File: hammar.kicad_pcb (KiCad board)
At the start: 2 copper layers, 97.5 x 53.8 mm, 115 parts, among them J1 Conn_01x08_Female, J10 YMIN, J11 ZMIN, J12 X, J13 Y, J14 Z, J15 E, J2 Conn_02x12_Odd_Even, J3 Z, J5 TEND, J7 TBED, J8 USB_C_Receptacle_USB2.0, J9 XMIN, Q1 Q_NMOS_GDS, Q2 Q_NMOS_GSD, Q3 Q_NMOS_GDS, SW1 SW_MEC_5G, SW2 SW_MEC_5G, U1 A4988, U2 ESP32-S2, U3 A4988, U4 A4988, U5 A4988, U6 3,3v lin, Y1 Crystal_GND24_Small

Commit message: Redesign
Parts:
- removed AE1: Antenna_Shield, MyAntennas:SWRU120B
- removed C11, C14, C5, C8, C9: 100nF, Capacitor_SMD:C_0603_1608Metric
- removed C16, C17: 1µF, Capacitor_SMD:C_0603_1608Metric
- removed C2: 15pF, Capacitor_SMD:C_0603_1608Metric
- removed C3: 1pF, Capacitor_SMD:C_0603_1608Metric
- removed SW2: SW_MEC_5G, Button_Switch_THT:SW_PUSH_6mm
- added G***: LOGO, LOGO, B.Cu at (110.8, 101.5)
- added J16: UART, Connector_PinHeader_2.54mm:PinHeader_1x04_P2.54mm_Vertical, B.Cu at (151.2, 99.7)
- added J6: Conn_01x03_Male, Connector_PinHeader_2.54mm:PinHeader_1x03_P2.54mm_Vertical, B.Cu at (97.3, 106.8)
- added Q4: Q_NPN_BEC, Package_TO_SOT_SMD:SOT-23, F.Cu at (137.7, 92.2)
- added Q5: Q_NPN_BEC, Package_TO_SOT_SMD:SOT-23, F.Cu at (133.7, 92.2)
- added R10: 22Ω, Resistor_SMD:R_0603_1608Metric, F.Cu at (172.0, 113.7)
- added R22: 1kΩ, Resistor_SMD:R_0603_1608Metric, F.Cu at (158.2, 113.0)
- added R34: 1kΩ, Resistor_SMD:R_0603_1608Metric, F.Cu at (123.0, 96.7)
- added R39: 680Ω, Resistor_SMD:R_0603_1608Metric, F.Cu at (106.8, 101.0)
- added R4: 22Ω, Resistor_SMD:R_0603_1608Metric, F.Cu at (172.0, 112.2)
- added R40: 10kΩ, Resistor_SMD:R_0603_1608Metric, F.Cu at (140.7, 92.2)
- added R41: 10kΩ, Resistor_SMD:R_0603_1608Metric, F.Cu at (130.7, 92.2)
- added R42: 10kΩ, Resistor_SMD:R_0603_1608Metric, F.Cu at (119.5, 102.2)
- added R43: 10kΩ, Resistor_SMD:R_0603_1608Metric, F.Cu at (121.5, 99.7)
- added U7: CH340G, Package_SO:SOIC-16_3.9x9.9mm_P1.27mm, F.Cu at (165.2, 113.0)
- added Z: ZMIN_probe, Connector_PinHeader_2.54mm:PinHeader_1x03_P2.54mm_Vertical, B.Cu at (101.7, 112.5)
- C1: value 15pF -> 100nF
- C15, C29, C30: footprint Capacitor_SMD:C_0603_1608Metric -> Capacitor_SMD:C_0805_2012Metric
- D5: value LED_Small -> D_Zener_~3,3v; footprint DIY:LED 0603 reverse mount -> Diode_SMD:D_SOD-323
- J11: value ZMIN -> I2C/SPI; footprint Connector_JST:JST_PH_S3B-PH-K_1x03_P2.00mm_Horizontal -> Connector_PinHeader_2.54mm:PinHeader_1x08_P2.54mm_Vertical; moved to B.Cu
- J12, J14, J15: footprint Connector_JST:JST_PH_S4B-PH-K_1x04_P2.00mm_Horizontal -> Connector_PinHeader_2.54mm:PinHeader_1x04_P2.54mm_Vertical; moved to B.Cu
- J2: value Conn_02x12_Odd_Even -> Micro_SD_Card; footprint Connector_PinHeader_2.54mm:PinHeader_2x12_P2.54mm_Vertical -> DIY:microSD
- J3: footprint Connector_JST:JST_PH_B4B-PH-K_1x04_P2.00mm_Vertical -> Connector_PinHeader_2.54mm:PinHeader_1x04_P2.54mm_Vertical; moved to B.Cu
- J5, J7: footprint Connector_JST:JST_PH_S2B-PH-K_1x02_P2.00mm_Horizontal -> Connector_PinHeader_2.54mm:PinHeader_1x02_P2.54mm_Vertical; moved to B.Cu
- Jw: renamed from J13; footprint Connector_JST:JST_PH_S4B-PH-K_1x04_P2.00mm_Horizontal -> Connector_PinHeader_2.54mm:PinHeader_1x04_P2.54mm_Vertical; moved to B.Cu
- R11: value 10kΩ -> 1kΩ
- R26: value 1kΩ -> 10kΩ
- SW1: moved to B.Cu
- U2: value ESP32-S2 -> ESP32-WROOM-32; footprint Package_DFN_QFN:QFN-56-1EP_7x7mm_P0.4mm_EP5.6x5.6mm -> RF_Module:ESP32-WROOM-32
- U6: footprint Package_TO_SOT_SMD:TO-252-2 -> DIY:mini BUCK
- X: renamed from J9; footprint Connector_JST:JST_PH_S3B-PH-K_1x03_P2.00mm_Horizontal -> Connector_PinHeader_2.54mm:PinHeader_1x03_P2.54mm_Vertical; moved to B.Cu
- Y: renamed from J10; footprint Connector_JST:JST_PH_S3B-PH-K_1x03_P2.00mm_Horizontal -> Connector_PinHeader_2.54mm:PinHeader_1x03_P2.54mm_Vertical; moved to B.Cu
- Y1: value Crystal_GND24_Small -> Resonator_Small; footprint Crystal:Crystal_SMD_3225-4Pin_3.2x2.5mm -> DIY:resonator_3,2x1,3
- moved R11 54.5 mm to (158.2, 111.2), turned to 0 degrees
- moved Y1 51.9 mm to (172.0, 116.5), turned to 90 degrees
- moved J11 45.2 mm to (127.2, 112.2), turned to 0 degrees
- moved C1 45.1 mm to (165.5, 117.7)
- moved R26 41.2 mm to (145.7, 91.7), turned to 0 degrees
- moved C15 41.1 mm to (151.5, 110.5), turned to 0 degrees
- moved C12 37.8 mm to (151.2, 112.2)
- moved U2 29.6 mm to (139.2, 104.7), turned to 180 degrees
- moved C32 26.8 mm to (159.2, 100.5), turned to 180 degrees
- moved R25 25.8 mm to (170.0, 106.2), turned to 90 degrees
- moved SW1 23.6 mm to (117.3, 100.0), turned to 90 degrees
- moved R15 23.1 mm to (124.5, 96.7)
- moved C37 22.9 mm to (158.2, 98.7), turned to 0 degrees
- moved C22 21.7 mm to (121.5, 96.7)
- moved Q2 21.6 mm to (171.2, 93.5)
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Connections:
- C1 pad 2: Net-(C1-Pad2) -> +3.3V
- C22 pad 2: RST -> Net-(C22-Pad2)
- D5 pad 1: Net-(D5-Pad1) -> Z-MIN
- D5 pad 2: IO13 -> GND
- F2 pad 2: BEDCONN-F -> VIN
- J1 pad 3: +VDC -> BEDCONN
- J1 pad 4: BEDCONN -> BEDCONN-F
- J11 pad 3: Z-MIN -> SCL
- J2 pad 1: IO33 -> unconnected-(J2-Pad1)
- J2 pad 2: IO46 -> SS
- J2 pad 3: IO32/SPID -> MOSI
- J2 pad 4: IO45 -> +3.3V
- J2 pad 5: IO31/SPIQ -> SCK
- J2 pad 6: IO44/U0RXD -> GND
- J2 pad 7: IO30/SPICLK -> MISO
- J2 pad 8: IO43/U0TXD -> unconnected-(J2-Pad8)
- J2 pad 9: IO29/SPICLK -> unconnected-(J2-Pad9)
- R11 pad 1: Net-(R11-Pad1) -> TX
- R11 pad 2: +3.3V -> Net-(R11-Pad2)
- R15 pad 2: RST -> Net-(C22-Pad2)
- R26 pad 2: Net-(D5-Pad1) -> Z-DIR
- SW1 pad 1: RST -> Net-(C22-Pad2)
- U2 pad 1: +3.3V -> GND
- U2 pad 10: Y-DIR -> E-EN
- U2 pad 11: Z-STP -> X-DIR
- U2 pad 12: Z-DIR -> X-STP
- U2 pad 13: E-STP -> Z-STP
- U2 pad 14: E-DIR -> Z-DIR
- U2 pad 15: E-EN -> GND
- U2 pad 16: T-BED -> FAN
- U2 pad 17: END -> unconnected-(U2-Pad17)
- U2 pad 18: IO13 -> unconnected-(U2-Pad18)
- U2 pad 19: FAN -> unconnected-(U2-Pad19)
- U2 pad 2: Net-(AE1-Pad1) -> +3.3V
- U2 pad 20: +3.3V -> unconnected-(U2-Pad20)
- U2 pad 21: Z-MIN -> unconnected-(U2-Pad21)
- U2 pad 22: BED -> unconnected-(U2-Pad22)
- U2 pad 23: unconnected-(U2-Pad23) -> Z-MIN
- U2 pad 24: Net-(R11-Pad1) -> END
- U2 pad 25: D- -> IO0
- U2 pad 26: D+ -> BED
- U2 pad 27: +3.3V -> E-STP
- U2 pad 28: IO21 -> E-DIR
- U2 pad 29: IO26/SPI_CS1 -> SS
- U2 pad 3: +3.3V -> RST
- U2 pad 30: unconnected-(U2-Pad30) -> SCK
- U2 pad 31: IO27/SPIHD -> MISO
- U2 pad 32: IO28/SPIWP -> unconnected-(U2-Pad32)
- U2 pad 33: IO29/SPICLK -> SDA
- U2 pad 34: IO30/SPICLK -> TX
- U2 pad 35: IO31/SPIQ -> RX
- U2 pad 36: IO32/SPID -> SCL
- U2 pad 37: IO33 -> MOSI
- U2 pad 38: X-MIN -> GND
- U2 pad 39: Y-MIN -> GND
- U2 pad 4: +3.3V -> T-END
- U2 pad 5: BOOT -> T-BED
- U2 pad 6: T-END -> X-MIN
- U2 pad 7: X-STP -> Y-MIN
- U2 pad 8: X-DIR -> Y-DIR
- Y1 pad 1: Net-(C2-Pad2) -> Net-(U7-Pad7)
- Y1 pad 3: Net-(C1-Pad2) -> Net-(U7-Pad8)
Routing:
- net +VDC: track 205.2 -> 274.1 mm, vias 19 -> 23
- net D+: track 82.5 -> 14.4 mm, vias 2 -> 0
- net D-: track 78.2 -> 13.8 mm, vias 2 -> 0
- net DTR: track 0.00 -> 54.9 mm, vias 0 -> 2
- net RTS: track 0.00 -> 47.6 mm, vias 0 -> 2
- net TX: track 0.00 -> 41.6 mm, vias 0 -> 3
- net RX: track 0.00 -> 41.1 mm, vias 0 -> 3
- net MISO: track 0.00 -> 39.1 mm, vias 0 -> 1
- net Net-(AE1-Pad1): track 38.0 -> 0.00 mm
- net BOOT: track 36.7 -> 0.00 mm, vias 1 -> 0
- net IO40/JTAG/MTDO: track 34.7 -> 0.00 mm, vias 1 -> 0
- net IO39/JTAG/MTCK: track 34.3 -> 0.00 mm, vias 1 -> 0
- net IO41/JTAG/MTDI: track 30.3 -> 0.00 mm, vias 1 -> 0
- net IO42/JTAG/MTMS: track 29.2 -> 0.00 mm, vias 1 -> 0
- net MOSI: track 0.00 -> 29.2 mm, vias 0 -> 2
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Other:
- board size 97.5 x 53.8 mm -> 97.5 x 55 mm
- board text added: "+ -"
- board text added: "- +"
- board text added: "0"
- board text added: "End"
- board text added: "Hammar v1,1"
- board text added: "MISO"
- board text added: "MOSI"
- board text added: "RX"
- board text added: "S"
- board text added: "SCK"
- board text added: "SCL"
- board text added: "SDA"
- board text added: "TX"
- board text added: "VCC"
- board text added: "VIN"
- board text added: "Z voltage 3,3V VIN"
- board text removed: "- VIN +"
- board text removed: "17"
- board text removed: "21"
- board text removed: "26"
- board text removed: "27"
- board text removed: "28"
- board text removed: "29"
- board text removed: "30"
- board text removed: "31"
- board text removed: "32"
- board text removed: "33"
- board text removed: "36"
- board text removed: "37"
- board text removed: "38"
- board text removed: "39"
- board text removed: "40"
- board text removed: "41"
- board text removed: "42"
- board text removed: "43"
- board text removed: "44"
- board text removed: "45"
- board text removed: "46"
- board text removed: "BED"
- board text removed: "END"
- board text removed: "Hammar v1"
- board text removed: "S GND 3,3V"
- board text removed: "Test"

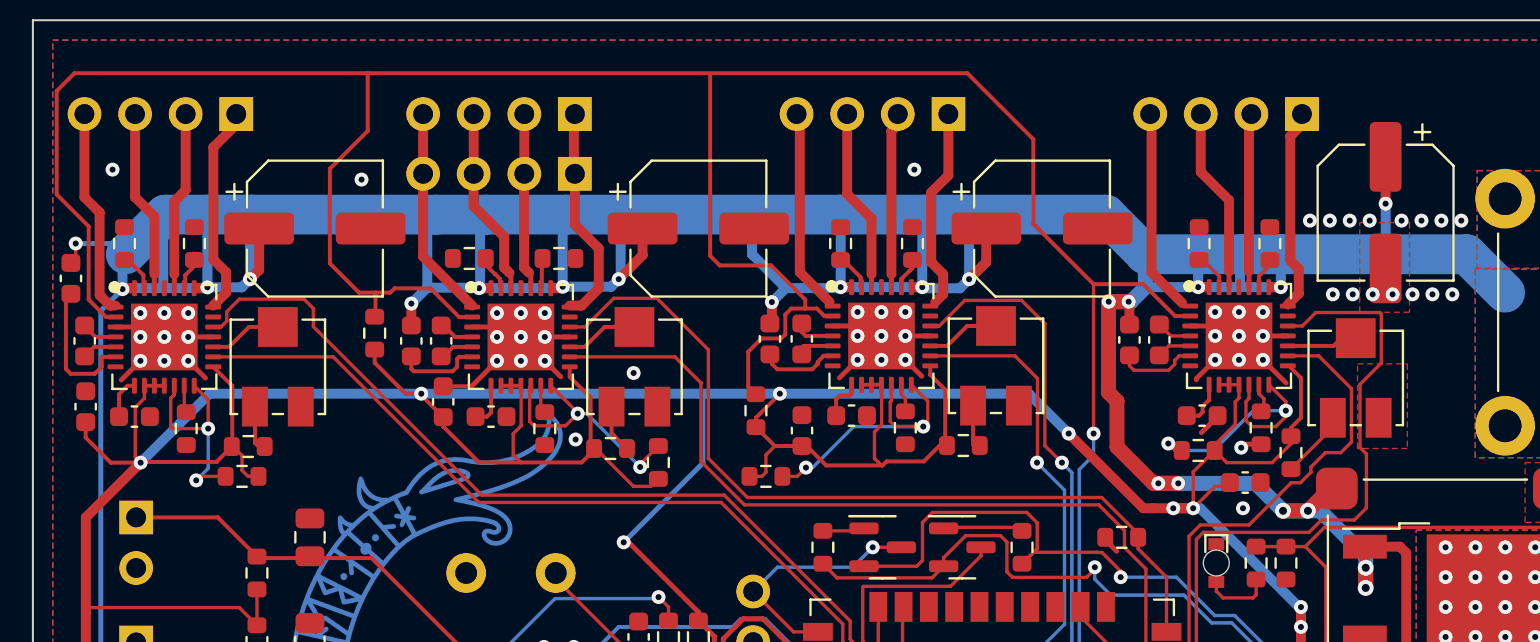
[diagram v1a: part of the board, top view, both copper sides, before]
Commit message: changed designators and updated BOM
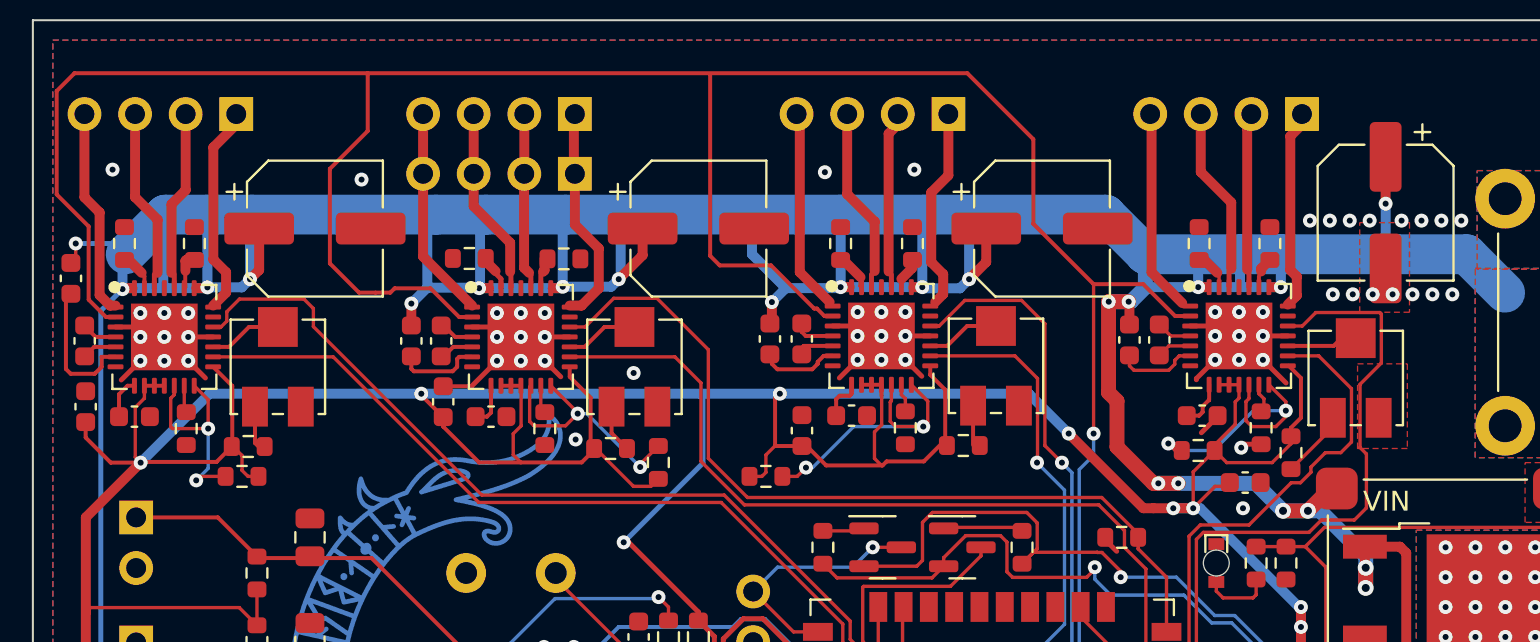
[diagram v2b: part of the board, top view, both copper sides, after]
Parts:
- removed the R34 at (108.2, 81.5)
- removed the R4 at (127.4, 85.4)
- D3: renamed from D5; value D_Zener_~3,3v -> Zener_~3,3v
- D6: value D_Small -> USB protection diode, >500mA 24V
- F1: value Fuse_Small -> 25A Mini fuse + Keystone 3557 fuse holders, or equivalent
- F2: value Fuse_Small -> 15A Mini fuse + Keystone 3557 fuse holders, or equivalent
- F3: value Polyfuse_Small -> Polyfuse 500mA
- J1: value Conn_01x08_Female -> 8x screw terminal, 5,08mm spacing. rated for >20A
- J2: value Micro_SD_Card -> Micro_SD_Holder
- Q1: renamed from Q5; value Q_NPN_BEC -> S9014 or equivalent
- Q2: renamed from Q4; value Q_NPN_BEC -> S9014 or equivalent
- Q3: renamed from Q2; value Q_NMOS_GSD -> TI CSD17310Q5A or equivalent
- Q4: renamed from Q1; value Q_NMOS_GDS -> PMV40UN2R or equivalent
- Q5: renamed from Q3; value Q_NMOS_GDS -> PMV40UN2R or equivalent
- RV1: renamed from RV2; value R_Potentiometer_Small -> Potentiometer_10kΩ
- RV2: renamed from RV4; value R_Potentiometer_Small -> Potentiometer_10kΩ
- RV3: value R_Potentiometer_Small -> Potentiometer_10kΩ
- RV4: renamed from RV1; value R_Potentiometer_Small -> Potentiometer_10kΩ
- RV5, RV6: value Varistor -> ESD varistor, optional
- U5: renamed from U6; value 3,3v lin -> DPAK 3,3v linear regulator + caps OR mini buck converter
- U6: renamed from U2; value ESP32-WROOM-32 -> ESP32-WROOM-32E
- Y1: value Resonator_Small -> Resonator_12mhz
- moved G*** 0.39 mm to (138.9, 100.6)
- moved R8 0.25 mm to (117.7, 77.7)
- renumbered C10 to C1, C31 to C10, C26 to C11, C24 to C12, C28 to C13, C36 to C14, C19 to C15, C6 to C16, C33 to C17, C25 to C18, C23 to C19, C35 to C2, C13 to C20, C29 to C21, C30 to C23, C37 to C24, C32 to C25, C15 to C26, C12 to C27, C1 to C28, C21 to C3, C27 to C4, C34 to C5, C20 to C6, C18 to C7, C7 to C8, C4 to C9, D2 to D1, D1 to D2, D3 to D4, D4 to D5, J7 to J10, J16 to J11, J6 to J12, J11 to J13, X to J14, Z to J15, Y to J16, J8 to J3, J12 to J4, Jw to J5, J14 to J6, J15 to J7, J3 to J8, J5 to J9, R37 to R1, R3 to R10, R33 to R11, R21 to R12, R8 to R13, R31 to R14, R18 to R15, R1 to R16, R2 to R17, R17 to R18, R30 to R19, R38 to R2, R7 to R20, R26 to R21, R41 to R22, R40 to R23, R19 to R24, R20 to R25, R29 to R26, R14 to R27, R13 to R28, R34 to R29, R12 to R3, R15 to R30, R32 to R31, R43 to R32, R39 to R33, R42 to R34, R24 to R35, R23 to R36, R25 to R37, R11 to R38, R4 to R39, R16 to R4, R35 to R40, R22 to R41, R10 to R42, R36 to R43, R27 to R7, R28 to R8, U3 to U1, U1 to U2, U5 to U3
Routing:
- net E-EN: track 146.4 -> 138.2 mm
- net +3.3V: track 380.3 -> 375.8 mm
- net GND: vias 96 -> 97
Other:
- board text added: "RST"

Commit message: little fix
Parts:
- J10: value TBED -> 1x2
- J11: value UART -> 1x4
- J12: value Conn_01x03_Male -> 1x3
- J13: value I2C/SPI -> 1x8
- J14: value XMIN -> 1x3
- J15: value ZMIN_probe -> 1x3
- J16: value YMIN -> 1x3
- J4: value X -> 1x4
- J5: value Y -> 1x4
- J6, J8: value Z -> 1x4
- J7: value E -> 1x4
- J9: value TEND -> 1x2
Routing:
- net E-EN: track 138.2 -> 137.4 mm

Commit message: updated bom++
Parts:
- D6: value USB protection diode, >500mA 24V -> USB protection diode, >500mA >24V. Silicon fine
- F1: value 25A Mini fuse + Keystone 3557 fuse holders, or equivalent -> 15A Mini fuse + Keystone 3557 fuse holders, or equivalent
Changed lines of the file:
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@@
       (effects (font (size 1 1) (thickness 0.15)))
     )
-    (fp_text value "USB protection diode, >500mA 24V" (at -0.25 2.25) (layer "F.Fab")
+    (fp_text value "USB protection diode, >500mA >24V. Silicon fine" (at -0.25 2.25) (layer "F.Fab")
       (effects (font (size 1 1) (thickness 0.15)))
     )
@@
       (effects (font (size 1 1) (thickness 0.15)))
     )
-    (fp_text value "25A Mini fuse + Keystone 3557 fuse holders, or equivalent" (at 0 -4 -90 unlocked) (layer "F.Fab")
-      (effects (font (size 1 1) (thickness 0.15)))
-    )
+    (fp_text value "15A Mini fuse + Keystone 3557 fuse holders, or equivalent" (at 0 -4 -90 unlocked) (layer "F.Fab")
+      (effects (font (size 1 1) (thickness 0.15)))
+    )

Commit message: slight reference update
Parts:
- moved J3 0.25 mm to (185.6, 115.0)
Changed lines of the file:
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@@
   )
   (footprint "Connector_USB:USB_C_Receptacle_HRO_TYPE-C-31-M-12" (layer "F.Cu")
-    (at 185.865 114.972756 90)
+    (at 185.615 114.972756 90)
     (descr "USB Type-C receptacle for USB 2.0 and PD, http://www.krhro.com/uploads/soft/180320/1-1P320120243.pdf")
     (tags "usb usb-c 2.0 pd")
@@
   (segment (start 117.305 93.80897) (end 117.305 93.512874) (width 0.17) (layer "F.Cu") (net 28))
   (segment (start 121.202709 97.460465) (end 118.6503 100.012874) (width 0.17) (layer "F.Cu") (net 28))
-  (segment (start 180.715 116.472756) (end 180.965 116.222756) (width 0.25) (layer "F.Cu") (net 29))
-  (segment (start 177.805 116.687874) (end 178.53 117.412874) (width 0.25) (layer "F.Cu") (net 29))
-  (segment (start 178.53 117.412874) (end 179.797462 117.412874) (width 0.25) (layer "F.Cu") (net 29))
-  (segment (start 180.965 116.222756) (end 181.82 116.222756) (width 0.25) (layer "F.Cu") (net 29))
-  (segment (start 179.797462 117.412874) (end 180.715 116.495336) (width 0.25) (layer "F.Cu") (net 29))
-  (segment (start 180.715 116.495336) (end 180.715 116.472756) (width 0.25) (layer "F.Cu") (net 29))
+  (segment (start 179.815 117.442756) (end 180.315 116.942756) (width 0.25) (layer "F.Cu") (net 29))
+  (segment (start 178.559882 117.442756) (end 179.815 117.442756) (width 0.25) (layer "F.Cu") (net 29))
+  (segment (start 180.545 116.222756) (end 181.82 116.222756) (width 0.25) (layer "F.Cu") (net 29))
+  (segment (start 180.315 116.452756) (end 180.545 116.222756) (width 0.25) (layer "F.Cu") (net 29))
+  (segment (start 177.805 116.687874) (end 178.559882 117.442756) (width 0.25) (layer "F.Cu") (net 29))
+  (segment (start 180.315 116.942756) (end 180.315 116.452756) (width 0.25) (layer "F.Cu") (net 29))
   (segment (start 179.805 112.512874) (end 180.514882 113.222756) (width 0.2) (layer "F.Cu") (net 31))
   (segment (start 177.805 113.337874) (end 178.63 112.512874) (width 0.2) (layer "F.Cu") (net 31))
@@
   (segment (start 176.036176 115.472756) (end 180.215 115.472756) (width 0.8) (layer "F.Cu") (net 48))
   (segment (start 179.305 115.722756) (end 181.82 115.722756) (width 0.25) (layer "F.Cu") (net 48))
+  (segment (start 180.735 114.722756) (end 180.215 115.242756) (width 0.25) (layer "F.Cu") (net 48))
+  (segment (start 181.82 114.722756) (end 180.735 114.722756) (width 0.25) (layer "F.Cu") (net 48))
   (segment (start 172.79 113.722756) (end 173.06 113.452756) (width 0.8) (layer "F.Cu") (net 48))
-  (segment (start 180.965 114.722756) (end 180.215 115.472756) (width 0.25) (layer "F.Cu") (net 48))
+  (segment (start 180.215 115.242756) (end 180.215 115.472756) (width 0.25) (layer "F.Cu") (net 48))
   (segment (start 173.06 113.452756) (end 174.016176 113.452756) (width 0.8) (layer "F.Cu") (net 48))
   (segment (start 174.016176 113.452756) (end 176.036176 115.472756) (width 0.8) (layer "F.Cu") (net 48))
-  (segment (start 181.82 114.722756) (end 180.965 114.722756) (width 0.25) (layer "F.Cu") (net 48))
   (segment (start 179.305 116.687874) (end 179.305 115.722756) (width 0.25) (layer "F.Cu") (net 48))
   (segment (start 106.045 100.907756) (end 106.045 102.907756) (width 0.17) (layer "F.Cu") (net 49))
